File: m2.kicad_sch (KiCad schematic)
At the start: 59 parts, among them J13 Bus_M.2_1-2199230-6, J14 Bus_M.2_2199230-2, Y3 Oscillator_32.768kHz_ECS_2520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

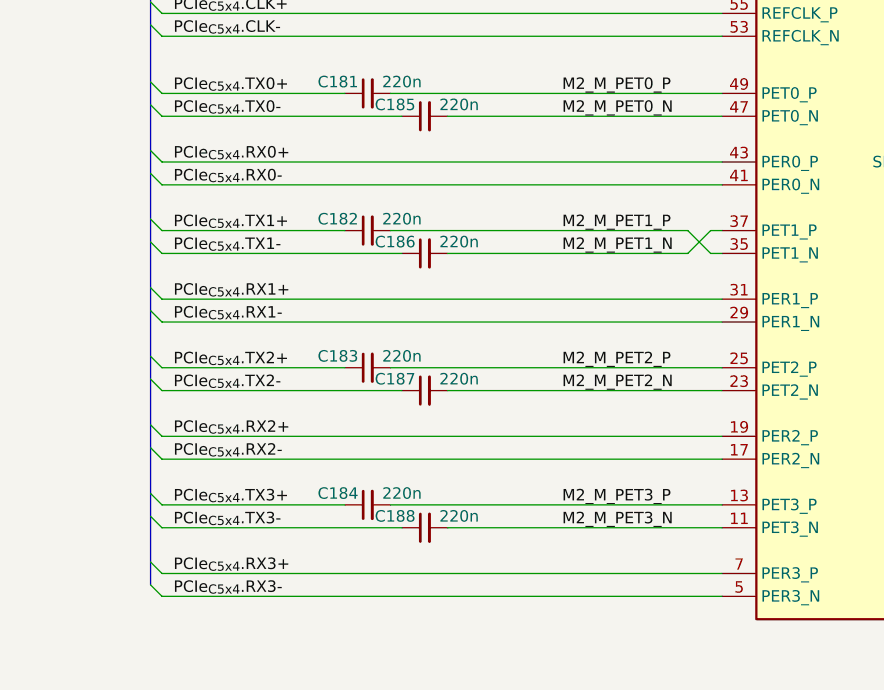
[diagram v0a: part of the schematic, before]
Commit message: [#83396] Route M.2 key M PCIe
[#83396] Define Net Classes for all interfaces
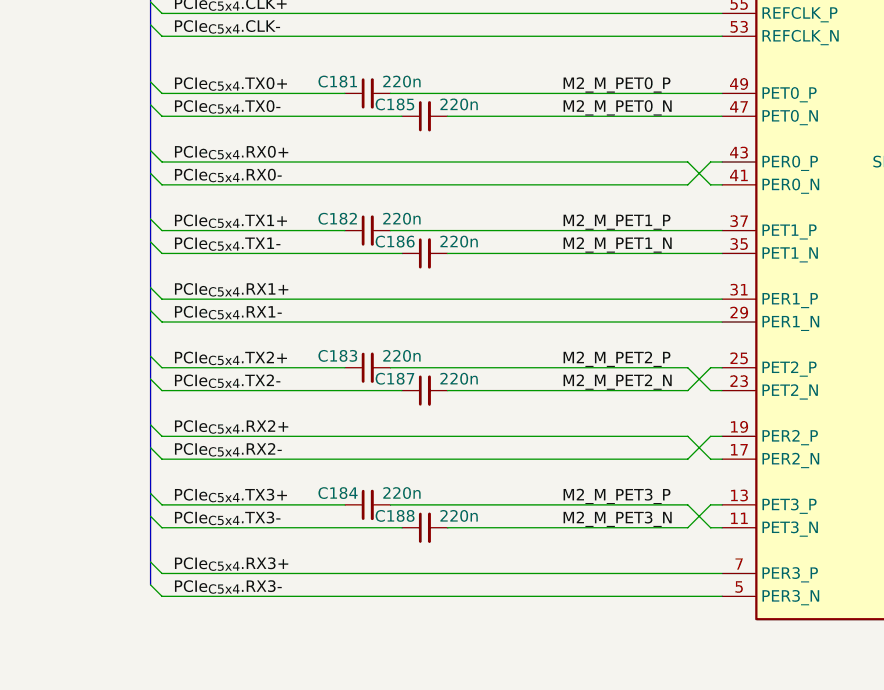
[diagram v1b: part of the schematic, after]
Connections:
- net M2_M_PET1_N: now also J13.35 (PET1_N); no longer J13.37 (PET1_P)
- net M2_M_PET1_P: now also J13.37 (PET1_P); no longer J13.35 (PET1_N)
- net M2_M_PET2_N: now also J13.25 (PET2_P); no longer J13.23 (PET2_N)
- net M2_M_PET2_P: now also J13.23 (PET2_N); no longer J13.25 (PET2_P)
- net M2_M_PET3_N: now also J13.13 (PET3_P); no longer J13.11 (PET3_N)
- net M2_M_PET3_P: now also J13.11 (PET3_N); no longer J13.13 (PET3_P)
- net PCIe_{C5x4}.RX0+: now also J13.41 (PER0_N); no longer J13.43 (PER0_P)
- net PCIe_{C5x4}.RX0-: now also J13.43 (PER0_P); no longer J13.41 (PER0_N)
- net PCIe_{C5x4}.RX2+: now also J13.17 (PER2_N); no longer J13.19 (PER2_P)
- net PCIe_{C5x4}.RX2-: now also J13.19 (PER2_P); no longer J13.17 (PER2_N)
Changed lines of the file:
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@@
+	(wire
+		(pts
+			(xy 96.52 132.08) (xy 99.06 134.62)
+		)
+		(stroke
+			(width 0)
+			(type default)
+		)
+	)
 	(wire
 		(pts
@@
 		)
 	)
+	(wire
+		(pts
+			(xy 99.06 172.72) (xy 100.33 172.72)
+		)
+		(stroke
+			(width 0)
+			(type default)
+		)
+	)
 	(bus
 		(pts
@@
 	(wire
 		(pts
-			(xy 38.1 132.08) (xy 100.33 132.08)
+			(xy 38.1 132.08) (xy 96.52 132.08)
 		)
 		(stroke
@@
 	(wire
 		(pts
+			(xy 96.52 154.94) (xy 99.06 157.48)
+		)
+		(stroke
+			(width 0)
+			(type default)
+		)
+	)
+	(wire
+		(pts
 			(xy 293.37 184.15) (xy 327.66 184.15)
 		)
@@
 	(wire
 		(pts
+			(xy 99.06 162.56) (xy 100.33 162.56)
+		)
+		(stroke
+			(width 0)
+			(type default)
+		)
+	)
+	(wire
+		(pts
 			(xy 38.1 124.46) (xy 58.42 124.46)
 		)
@@
 	(wire
 		(pts
+			(xy 99.06 165.1) (xy 100.33 165.1)
+		)
+		(stroke
+			(width 0)
+			(type default)
+		)
+	)
+	(wire
+		(pts
 			(xy 226.06 111.76) (xy 262.89 111.76)
 		)
@@
 	(wire
 		(pts
-			(xy 69.85 142.24) (xy 96.52 142.24)
+			(xy 69.85 142.24) (xy 100.33 142.24)
 		)
 		(stroke
@@
 	(wire
 		(pts
-			(xy 63.5 139.7) (xy 96.52 139.7)
+			(xy 63.5 139.7) (xy 100.33 139.7)
 		)
 		(stroke
@@
 	(wire
 		(pts
-			(xy 38.1 165.1) (xy 100.33 165.1)
+			(xy 96.52 162.56) (xy 99.06 165.1)
+		)
+		(stroke
+			(width 0)
+			(type default)
+		)
+	)
+	(wire
+		(pts
+			(xy 38.1 165.1) (xy 96.52 165.1)
 		)
 		(stroke
@@
 	(wire
 		(pts
+			(xy 99.06 170.18) (xy 100.33 170.18)
+		)
+		(stroke
+			(width 0)
+			(type default)
+		)
+	)
+	(wire
+		(pts
 			(xy 38.1 142.24) (xy 64.77 142.24)
 		)
@@
 	(wire
 		(pts
-			(xy 69.85 172.72) (xy 100.33 172.72)
+			(xy 69.85 172.72) (xy 96.52 172.72)
 		)
 		(stroke
@@
 	(wire
 		(pts
+			(xy 96.52 170.18) (xy 99.06 172.72)
+		)
+		(stroke
+			(width 0)
+			(type default)
+		)
+	)
+	(wire
+		(pts
 			(xy 38.1 102.87) (xy 62.23 102.87)
 		)
@@
 		)
 	)
+	(wire
+		(pts
+			(xy 96.52 157.48) (xy 99.06 154.94)
+		)
+		(stroke
+			(width 0)
+			(type default)
+		)
+	)
 	(polyline
 		(pts
@@
 	(wire
 		(pts
-			(xy 63.5 154.94) (xy 100.33 154.94)
+			(xy 63.5 154.94) (xy 96.52 154.94)
 		)
 		(stroke
@@
 	(wire
 		(pts
+			(xy 96.52 134.62) (xy 99.06 132.08)
+		)
+		(stroke
+			(width 0)
+			(type default)
+		)
+	)
+	(wire
+		(pts
 			(xy 135.89 262.89) (xy 120.65 262.89)
 		)
@@
 	(wire
 		(pts
-			(xy 38.1 134.62) (xy 100.33 134.62)
+			(xy 38.1 134.62) (xy 96.52 134.62)
 		)
 		(stroke
@@
 	(wire
 		(pts
-			(xy 38.1 162.56) (xy 100.33 162.56)
+			(xy 38.1 162.56) (xy 96.52 162.56)
 		)
 		(stroke
@@
 	(wire
 		(pts
-			(xy 63.5 170.18) (xy 100.33 170.18)
+			(xy 63.5 170.18) (xy 96.52 170.18)
 		)
 		(stroke
@@
 	(wire
 		(pts
-			(xy 96.52 139.7) (xy 99.06 142.24)
+			(xy 99.06 134.62) (xy 100.33 134.62)
 		)
 		(stroke
@@
 	(wire
 		(pts
+			(xy 99.06 157.48) (xy 100.33 157.48)
+		)
+		(stroke
+			(width 0)
+			(type default)
+		)
+	)
+	(wire
+		(pts
 			(xy 314.96 134.62) (xy 318.77 134.62)
 		)
@@
 	(wire
 		(pts
-			(xy 99.06 142.24) (xy 100.33 142.24)
+			(xy 96.52 165.1) (xy 99.06 162.56)
 		)
 		(stroke
@@
 	(wire
 		(pts
-			(xy 99.06 139.7) (xy 100.33 139.7)
+			(xy 96.52 172.72) (xy 99.06 170.18)
 		)
 		(stroke
@@
 	(wire
 		(pts
+			(xy 99.06 154.94) (xy 100.33 154.94)
+		)
+		(stroke
+			(width 0)
+			(type default)
+		)
+	)
+	(wire
+		(pts
+			(xy 99.06 132.08) (xy 100.33 132.08)
+		)
+		(stroke
+			(width 0)
+			(type default)
+		)
+	)
+	(wire
+		(pts
 			(xy 241.3 165.1) (xy 262.89 165.1)
 		)
@@
 	(wire
 		(pts
-			(xy 69.85 157.48) (xy 100.33 157.48)
+			(xy 69.85 157.48) (xy 96.52 157.48)
 		)
 		(stroke
@@
 		)
 		(stroke
-			(width 0)
-			(type default)
-		)
-	)
-	(wire
-		(pts
-			(xy 96.52 142.24) (xy 99.06 139.7)
-		)
-		(stroke

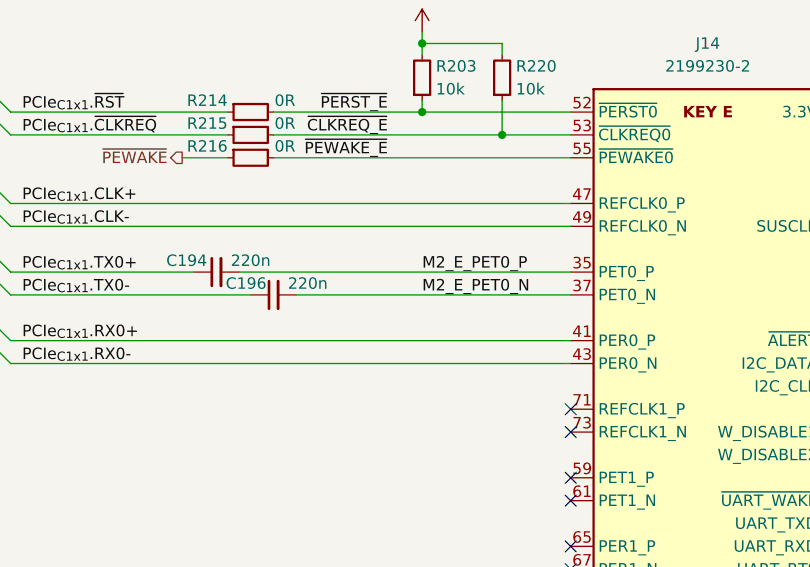
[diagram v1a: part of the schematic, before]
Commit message: [#83396] Route M.2 key E PCIe
[#83396] Define Net Classes for all interfaces
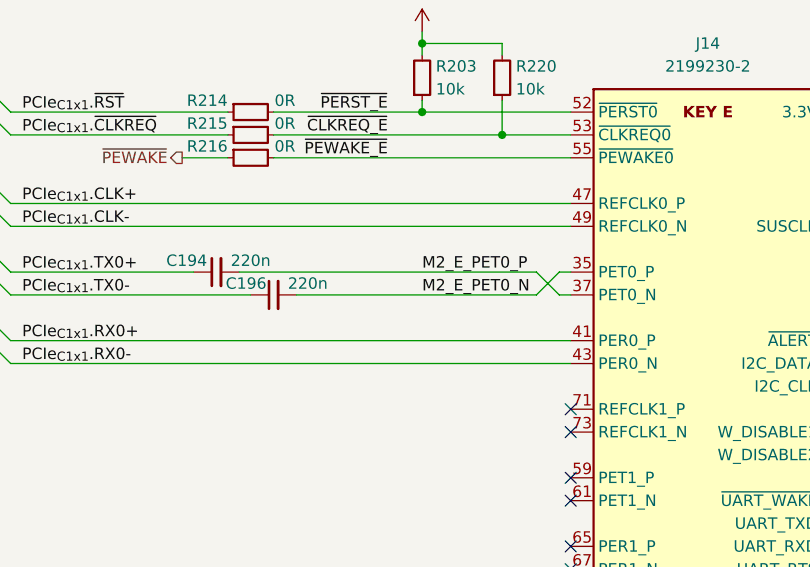
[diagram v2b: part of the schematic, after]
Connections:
- net M2_E_PET0_N: now also J14.35 (PET0_P); no longer J14.37 (PET0_N)
- net M2_E_PET0_P: now also J14.37 (PET0_N); no longer J14.35 (PET0_P)
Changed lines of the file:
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@@
 	(wire
 		(pts
-			(xy 226.06 111.76) (xy 262.89 111.76)
+			(xy 226.06 111.76) (xy 259.08 111.76)
 		)
 		(stroke
@@
 	(wire
 		(pts
-			(xy 232.41 114.3) (xy 262.89 114.3)
+			(xy 232.41 114.3) (xy 259.08 114.3)
 		)
 		(stroke
@@
 	(wire
 		(pts
+			(xy 259.08 111.76) (xy 261.62 114.3)
+		)
+		(stroke
+			(width 0)
+			(type default)
+		)
+	)
+	(wire
+		(pts
 			(xy 135.89 262.89) (xy 120.65 262.89)
 		)
@@
 	(wire
 		(pts
+			(xy 259.08 114.3) (xy 261.62 111.76)
+		)
+		(stroke
+			(width 0)
+			(type default)
+		)
+	)
+	(wire
+		(pts
 			(xy 137.16 99.06) (xy 137.16 100.33)
 		)
@@
 		)
 	)
+	(wire
+		(pts
+			(xy 261.62 111.76) (xy 262.89 111.76)
+		)
+		(stroke
+			(width 0)
+			(type default)
+		)
+	)
 	(bus
 		(pts
@@
 		)
 		(stroke
+			(width 0)
+			(type default)
+		)
+	)
+	(wire
+		(pts
+			(xy 261.62 114.3) (xy 262.89 114.3)
+		)
+		(stroke

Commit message: [#83396] WIP: Route CSI
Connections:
- net PCIe_{C1x1}.CLK+: now also J14.49 (REFCLK0_N); no longer J14.47 (REFCLK0_P)
- net PCIe_{C1x1}.CLK-: now also J14.47 (REFCLK0_P); no longer J14.49 (REFCLK0_N)
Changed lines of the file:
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@@
+	(wire
+		(pts
+			(xy 261.62 104.14) (xy 262.89 104.14)
+		)
+		(stroke
+			(width 0)
+			(type default)
+		)
+	)
 	(wire
 		(pts
@@
 	(wire
 		(pts
+			(xy 259.08 106.68) (xy 261.62 104.14)
+		)
+		(stroke
+			(width 0)
+			(type default)
+		)
+	)
+	(wire
+		(pts
 			(xy 63.5 124.46) (xy 100.33 124.46)
 		)
@@
 		)
 	)
+	(wire
+		(pts
+			(xy 259.08 104.14) (xy 261.62 106.68)
+		)
+		(stroke
+			(width 0)
+			(type default)
+		)
+	)
 	(bus
 		(pts
@@
 	(wire
 		(pts
+			(xy 261.62 106.68) (xy 262.89 106.68)
+		)
+		(stroke
+			(width 0)
+			(type default)
+		)
+	)
+	(wire
+		(pts
 			(xy 295.91 86.36) (xy 300.99 86.36)
 		)
@@
 	(wire
 		(pts
-			(xy 200.66 104.14) (xy 262.89 104.14)
+			(xy 200.66 104.14) (xy 259.08 104.14)
 		)
 		(stroke
@@
 	(wire
 		(pts
-			(xy 200.66 106.68) (xy 262.89 106.68)
-		)
-		(stroke
+			(xy 200.66 106.68) (xy 259.08 106.68)
+		)
+		(stroke

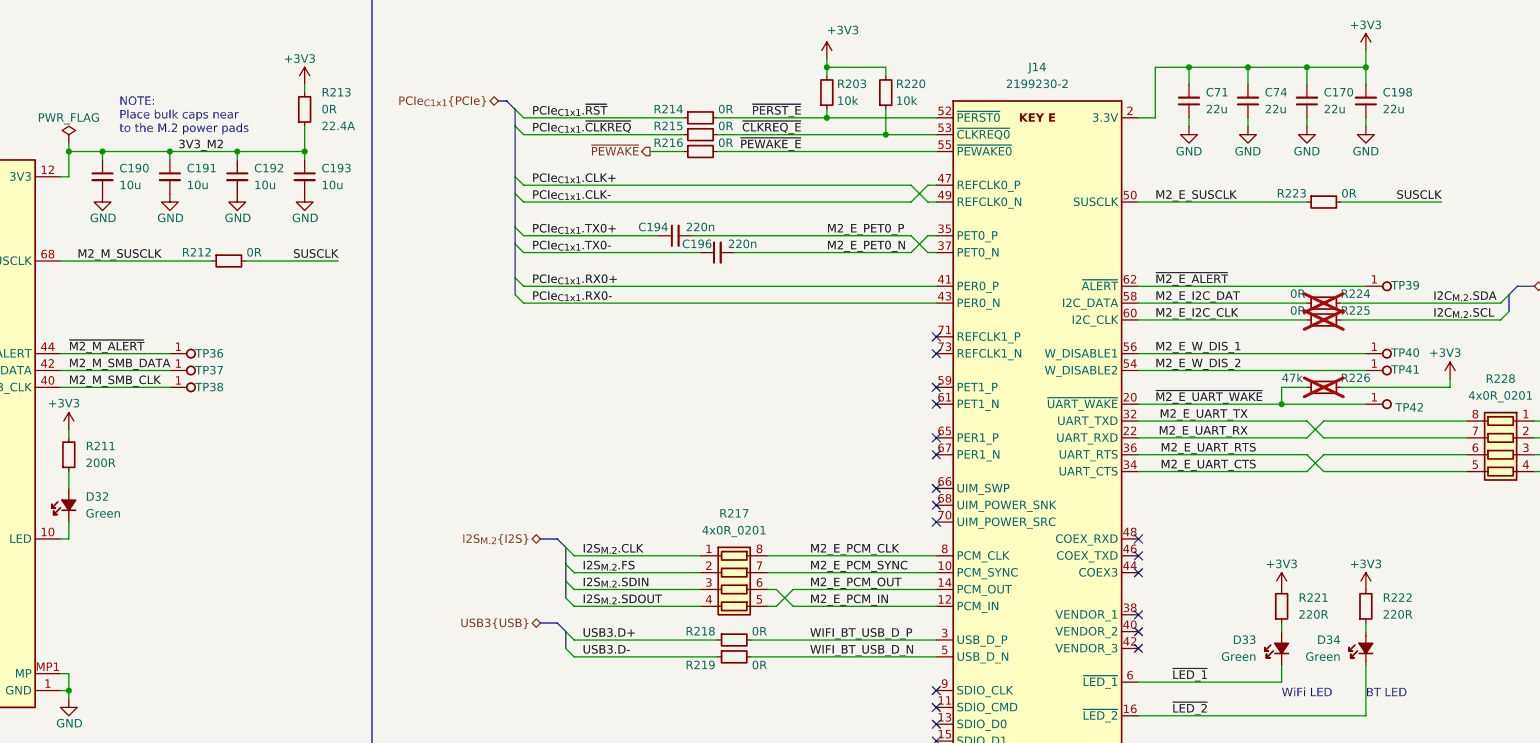
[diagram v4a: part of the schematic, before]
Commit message: [#83396] Implement small post review fixes eg. correct LED resistor values, update sheet table, delete four wire connections
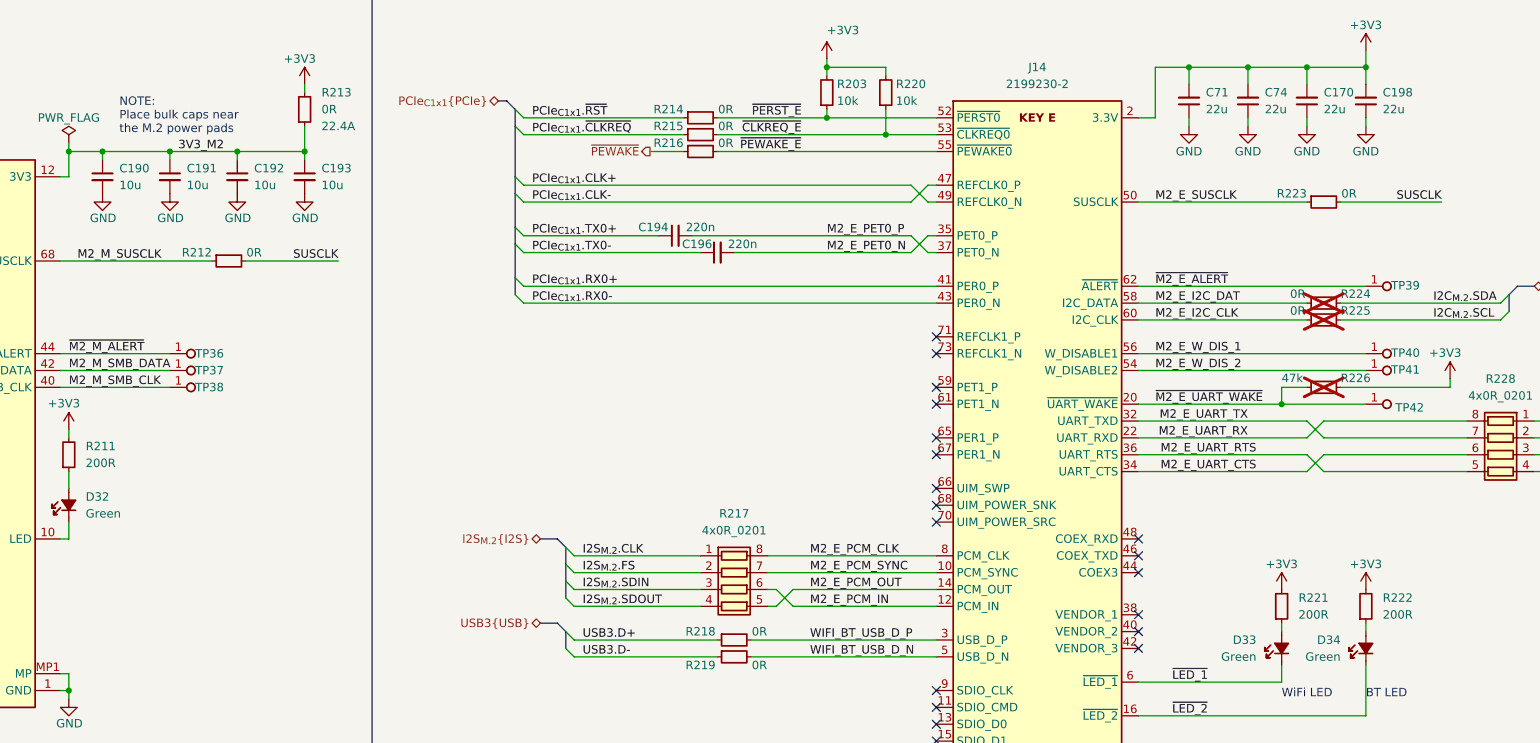
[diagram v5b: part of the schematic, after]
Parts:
- removed R221, R222: R_220R_0402, antmicro-footprints:R_0402_1005Metric, symbol antmicroResistors0402:R_220R_0402
- added R221, R222: R_200R_0402, antmicro-footprints:R_0402_1005Metric, symbol antmicroResistors0402:R_200R_0402
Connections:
- net +3V3: now also R221.2, R222.2
- net at D34.2 (A): now also R222.1
- net at D33.2 (A): now also R221.1
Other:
- note added: "NOTE: Place bulk caps near the M.2 power pads"
- note removed: "NOTE: Place bulk caps near to the M.2 power pads"

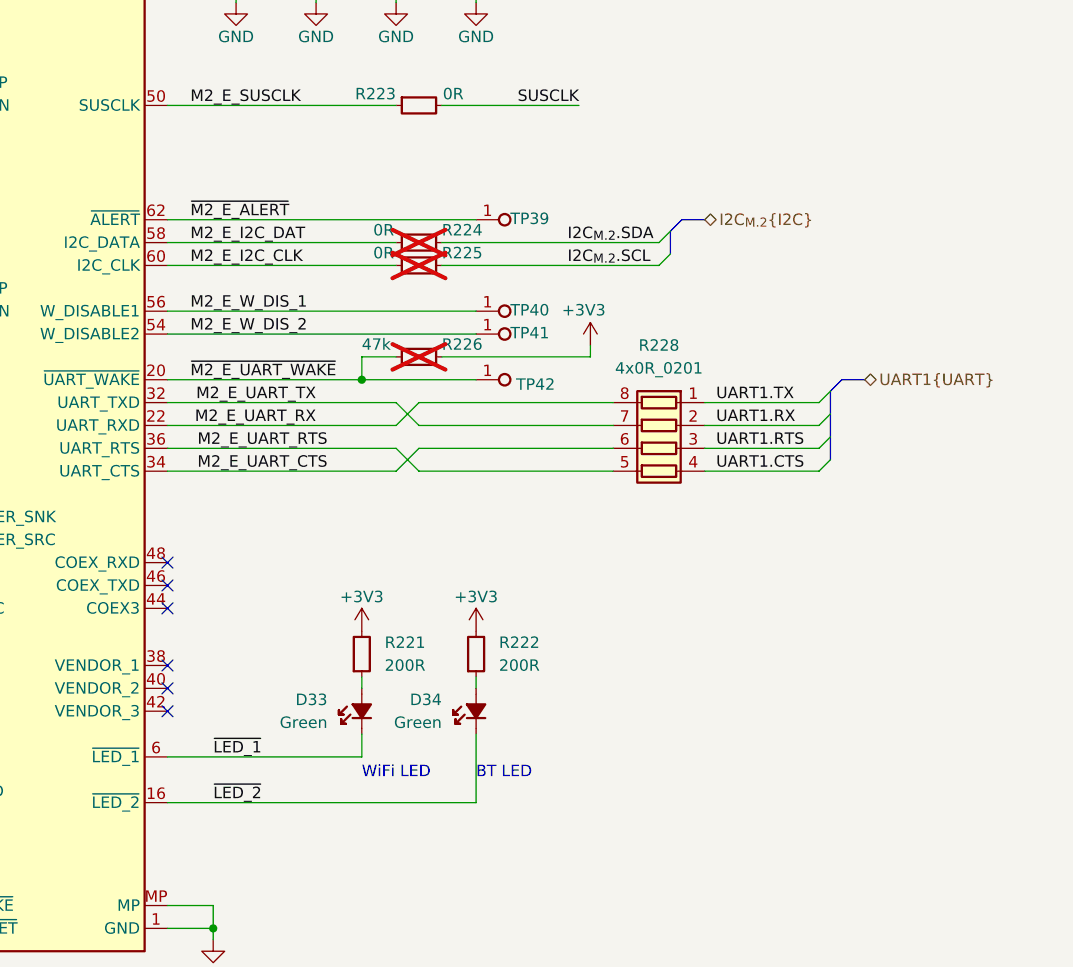
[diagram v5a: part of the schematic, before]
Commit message: [#83396] Continue post review fixes according power and M.2
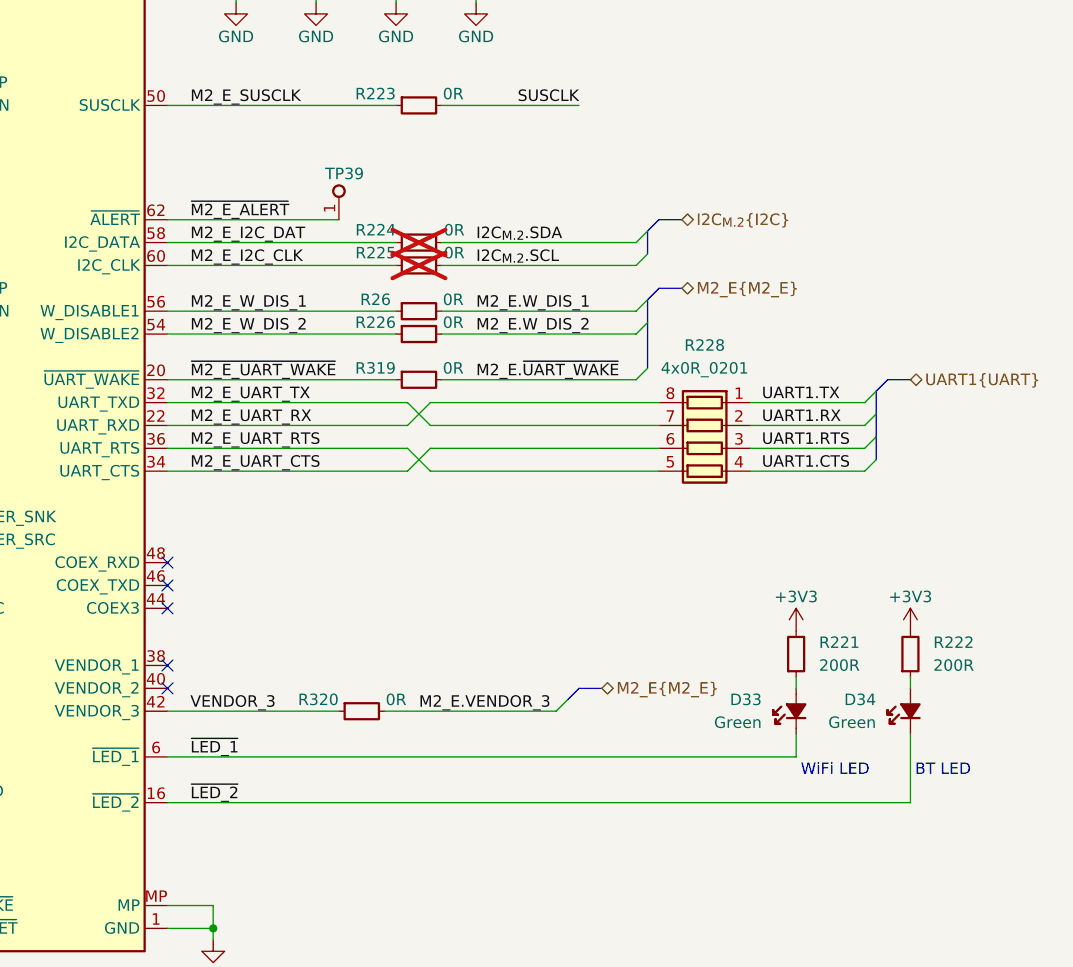
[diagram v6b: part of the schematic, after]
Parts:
- removed R226: R_47k_0402, antmicro-footprints:R_0402_1005Metric, symbol antmicroResistors0402:R_47k_0402
- removed TP40, TP41, TP42: TP_0.75mm_SMD, antmicro-footprints:TP_SMD_0.75mm, symbol antmicroTestPoints:TP_0.75mm_SMD
- added R226, R26, R319, R320: R_0R_0402, antmicro-footprints:R_0402_1005Metric, symbol antmicroResistors0402:R_0R_0402
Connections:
- net I2C_{M.2}.SCL: now also R225.1; no longer R225.2
- net I2C_{M.2}.SDA: now also R224.1; no longer R224.2
- net M2_E_I2C_CLK: now also R225.2; no longer R225.1
- net M2_E_I2C_DAT: now also R224.2; no longer R224.1
- net M2_E_W_DIS_1: now also R26.1
- net M2_E_W_DIS_2: now also R226.1
- net ~{M2_E_UART_WAKE}: now also R319.1
- net VENDOR_3: now reaches J14.42 (VENDOR_3)
- net VENDOR_3: now also R320.1
- new net M2_E.VENDOR_3: R320.2
- new net M2_E.W_DIS_1: R26.2
- new net M2_E.W_DIS_2: R226.2
- new net M2_E.~{UART_WAKE}: R319.2
- no-connect marks 23 -> 22
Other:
- moved on the sheet: D33, D34, R221, R222, R228, TP39
